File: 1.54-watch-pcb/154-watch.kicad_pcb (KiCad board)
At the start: 4 copper layers, 49.5 x 33 mm, 58 parts, among them J1 AFC24-S24FIC-00, J2 Conn_01x06_Female, J3 USB_C_Programming, J4 Jack-DC, J5 Conn_01x02_Male, Q1 Si1308, Q2 BC817, Q3 BC817, Q4 Si2301CDS, SW1 RESET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

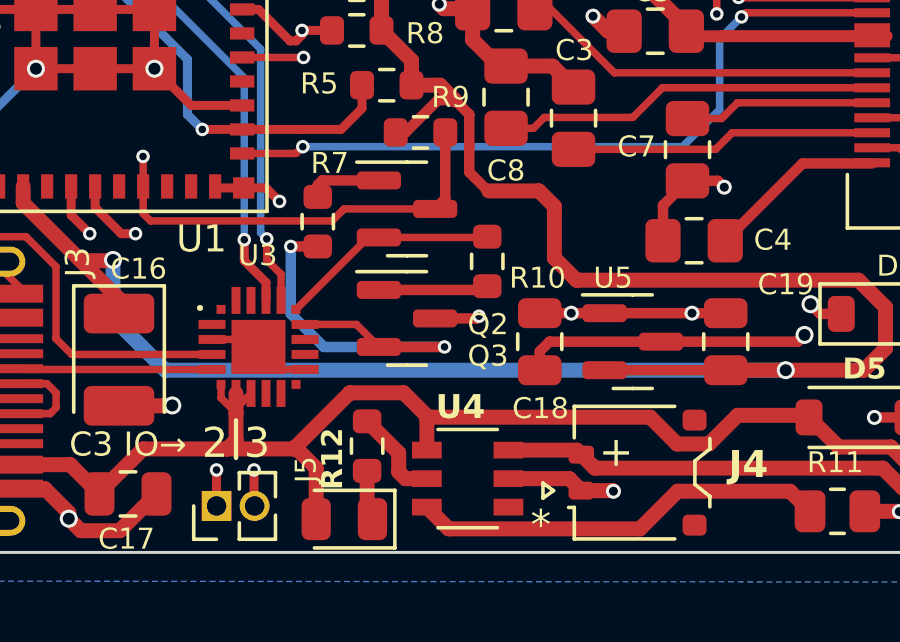
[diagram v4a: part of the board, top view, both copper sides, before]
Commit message: #6 Add a pull-down to power switch Q4
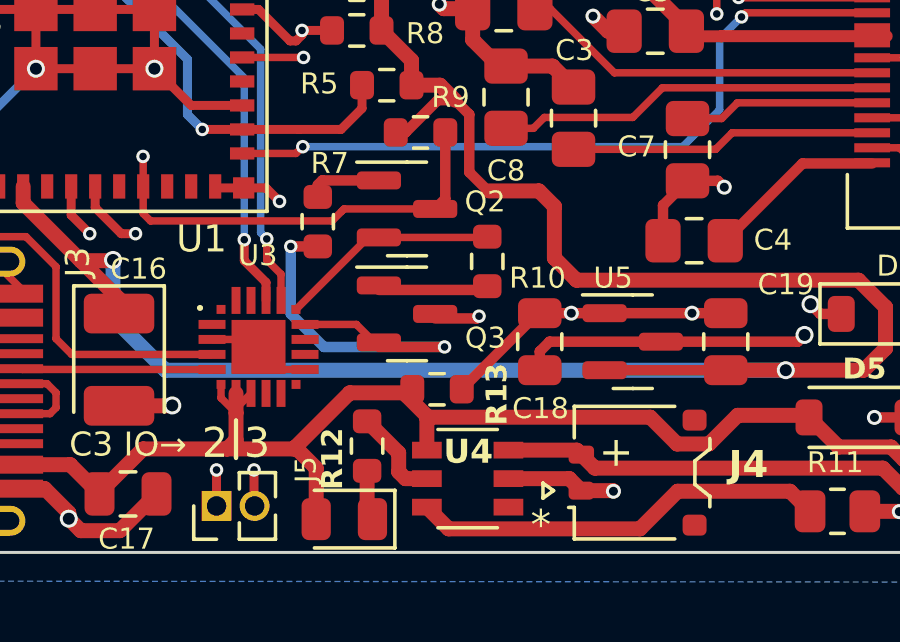
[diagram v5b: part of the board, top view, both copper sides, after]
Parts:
- added R13: 10K, Resistor_SMD:R_0603_1608Metric, F.Cu at (94.7, 57.1)
- moved Q3 0.15 mm to (93.7, 54.5)
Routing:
- net GND: track 101.2 -> 104.9 mm
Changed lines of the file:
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@@
     )
     (pad_to_mask_clearance 0)
-    (grid_origin 111.4 43.762)
     (pcbplotparams
       (layerselection 0x00010fc_ffffffff)
@@
   )
   (footprint "Package_TO_SOT_SMD:SOT-23" (layer "F.Cu")
-    (at 93.7 54.7)
+    (at 93.7 54.55)
     (descr "SOT, 3 Pin (https://www.jedec.org/system/files/docs/to-236h.pdf variant AB), generated with kicad-footprint-generator ipc_gullwing_generator.py")
     (tags "SOT TO_SOT_SMD")
@@
     (property "ki_keywords" "NPN Transistor")
     (attr smd)
-    (fp_text reference "Q3" (at 2.7 1.25) (layer "F.SilkS")
+    (fp_text reference "Q3" (at 2.61 0.8) (layer "F.SilkS")
         (effects (font (size 0.7 0.7) (thickness 0.13)))
     )
@@
     )
   )
+  (footprint "Resistor_SMD:R_0603_1608Metric" (layer "F.Cu")
+    (at 94.7 57.06 180)
+    (descr "Resistor SMD 0603 (1608 Metric), square (rectangular) end terminal, IPC_7351 nominal, (Body size source: IPC-SM-782 page 72, https://www.pcb-3d.com/wordpress/wp-content/uploads/ipc-sm-782a_amendment_1_and_2.pdf), generated with kicad-footprint-generator")
+    (tags "resistor")
+    (property "LCSC" "C25804")
+    (property "Sheetfile" "154-watch.kicad_sch")
+    (property "Sheetname" "")
+    (property "ki_description" "Resistor, small symbol")
+    (property "ki_keywords" "R resistor")
+    (attr smd)
+    (fp_text reference "R13" (at -1.99 -0.17 90) (layer "F.SilkS")
+        (effects (font (size 0.7 0.7) (thickness 0.13) bold))
+    )
+    (fp_text value "10K" (at 0 1.43) (layer "F.Fab")
+        (effects (font (size 1 1) (thickness 0.15)))
+    )
+    (fp_text user "${REFERENCE}" (at 0 0) (layer "F.Fab")
+        (effects (font (size 0.4 0.4) (thickness 0.06)))
+    )
+    (fp_line (start -0.237258 -0.5225) (end 0.237258 -0.5225)
+      (stroke (width 0.12) (type solid)) (layer "F.SilkS"))
+    (fp_line (start -0.237258 0.5225) (end 0.237258 0.5225)
+      (stroke (width 0.12) (type solid)) (layer "F.SilkS"))
+    (fp_line (start -1.48 -0.73) (end 1.48 -0.73)
+      (stroke (width 0.05) (type solid)) (layer "F.CrtYd"))
+    (fp_line (start -1.48 0.73) (end -1.48 -0.73)
+      (stroke (width 0.05) (type solid)) (layer "F.CrtYd"))
+    (fp_line (start 1.48 -0.73) (end 1.48 0.73)
+      (stroke (width 0.05) (type solid)) (layer "F.CrtYd"))
+    (fp_line (start 1.48 0.73) (end -1.48 0.73)
+      (stroke (width 0.05) (type solid)) (layer "F.CrtYd"))
+    (fp_line (start -0.8 -0.4125) (end 0.8 -0.4125)
+      (stroke (width 0.1) (type solid)) (layer "F.Fab"))
+    (fp_line (start -0.8 0.4125) (end -0.8 -0.4125)
+      (stroke (width 0.1) (type solid)) (layer "F.Fab"))
+    (fp_line (start 0.8 -0.4125) (end 0.8 0.4125)
+      (stroke (width 0.1) (type solid)) (layer "F.Fab"))
+    (fp_line (start 0.8 0.4125) (end -0.8 0.4125)
+      (stroke (width 0.1) (type solid)) (layer "F.Fab"))
+    (pad "1" smd roundrect (at -0.825 0 180) (size 0.8 0.95) (layers "F.Cu" "F.Paste" "F.Mask") (roundrect_rratio 0.25)
+      (net 2 "GND") (pintype "passive"))
+    (pad "2" smd roundrect (at 0.825 0 180) (size 0.8 0.95) (layers "F.Cu" "F.Paste" "F.Mask") (roundrect_rratio 0.25)
+      (net 3 "VBUS") (pintype "passive"))
+    (model "${KICAD6_3DMODEL_DIR}/Resistor_SMD.3dshapes/R_0603_1608Metric.wrl"
+      (offset (xyz 0 0 0))
+      (scale (xyz 1 1 1))
+      (rotate (xyz 0 0 0))
+    )
+  )
   (footprint "Capacitor_SMD:C_0805_2012Metric_Pad1.18x1.45mm_HandSolder" (layer "F.Cu")
     (at 97 47.325 -90)
@@
     (property "ki_keywords" "NPN Transistor")
     (attr smd)
-    (fp_text reference "Q2" (at 2.7 3.85) (layer "F.SilkS")
+    (fp_text reference "Q2" (at 2.6 -0.24) (layer "F.SilkS")
         (effects (font (size 0.7 0.7) (thickness 0.13)))
     )
@@
     (property "Sheetname" "")
     (attr smd)
-    (fp_text reference "U4" (at 0.24 2.39 180) (layer "F.SilkS")
+    (fp_text reference "U4" (at -0.0189 0.900001 180) (layer "F.SilkS")
         (effects (font (size 0.8 0.8) (thickness 0.14) bold))
     )
@@
   (segment (start 94.925 44.375) (end 94.775 44.225) (width 0.5) (layer "F.Cu") (net 2))
   (segment (start 80.845 53.875) (end 80.845 53.72) (width 0.25) (layer "F.Cu") (net 2))
+  (segment (start 98.06 54.525) (end 95.525 57.06) (width 0.35) (layer "F.Cu") (net 2))
   (segment (start 86.5 31.75) (end 86.75 32) (width 0.3) (layer "F.Cu") (net 2))
   (segment (start 89.55 38.45) (end 89.575 38.425) (width 0.35) (layer "F.Cu") (net 2))
@@
   (segment (start 80.845 53.72) (end 79.93 52.805) (width 0.25) (layer "F.Cu") (net 2))
   (segment (start 81.3301 42.425) (end 85.2801 42.425) (width 0.3) (layer "F.Cu") (net 2))
+  (segment (start 98.125 54.525) (end 98.06 54.525) (width 0.35) (layer "F.Cu") (net 2))
   (segment (start 80.2 36.45) (end 81.525 36.45) (width 0.25) (layer "F.Cu") (net 2))
   (segment (start 82.825 61.775) (end 82.425 61.375) (width 0.5) (layer "F.Cu") (net 2))

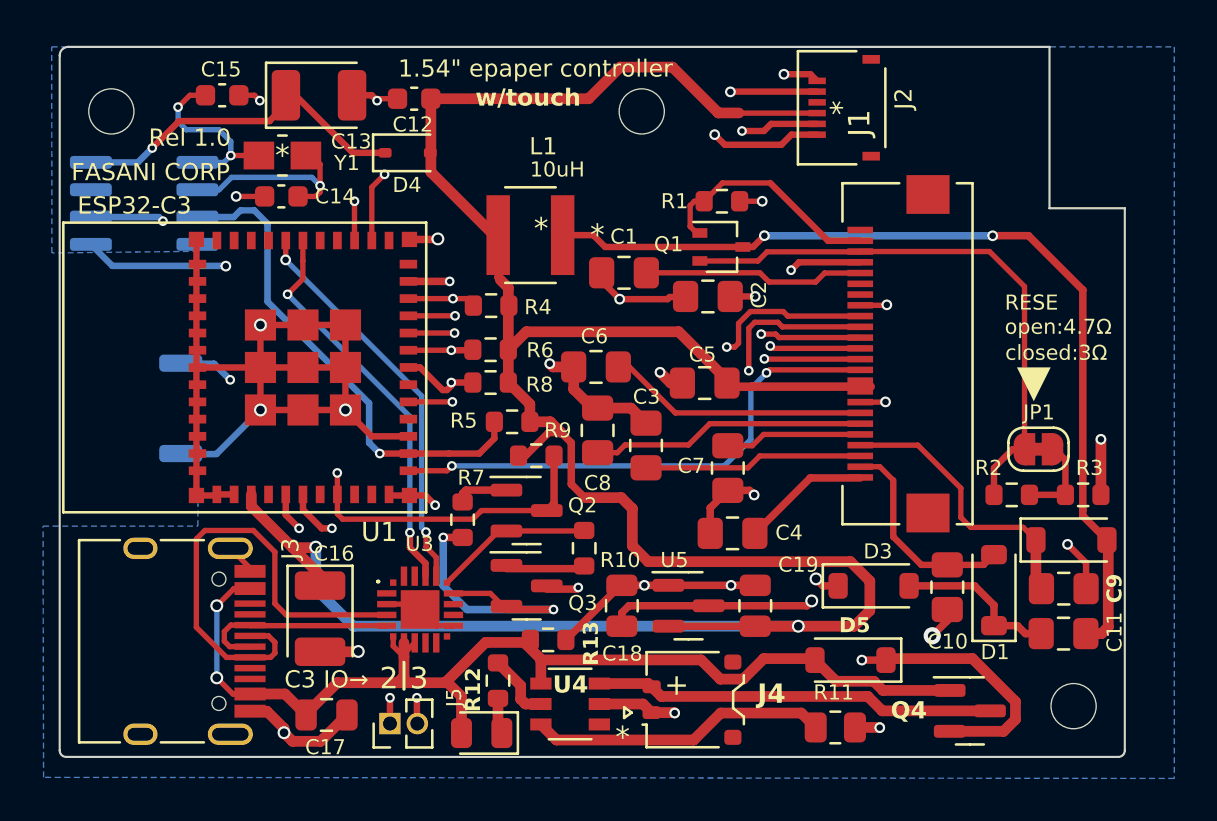
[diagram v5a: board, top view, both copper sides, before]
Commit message: Fix DRC 1.54 DRC
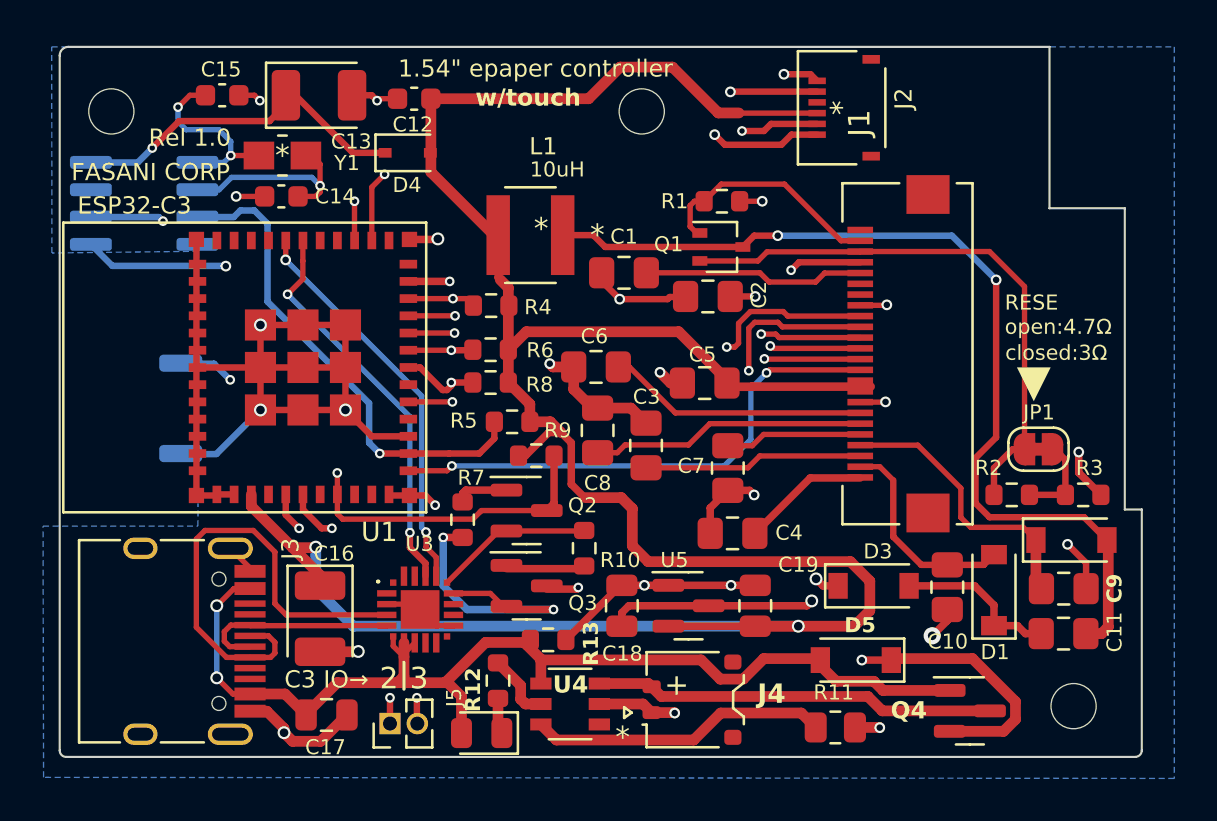
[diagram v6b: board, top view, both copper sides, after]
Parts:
- J1: value AFC24-S24FIC-00 -> CONN_AFC24-S24FIC-00_JUS
- U1: value ESP32-C3-MINI-1-N4 -> ESP32-C3-MINI
- U4: value TP4057-42-SOT26-R -> SOT-23-5_TPW
- moved D5 0.25 mm to (109.0, 58.0)
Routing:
- net Net-(D2-A): track 43.0 -> 44.3 mm
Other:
- board size 49.5 x 33 mm -> 50.3 x 33 mm

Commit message: 1.54 add QR code to this repo
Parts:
- moved SW1 3.58 mm to (76.1, 43.0), turned to 0 degrees
- moved H1 0.50 mm to (74.4, 32.0)
- moved H3 0.50 mm to (99.0, 32.0)
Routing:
- net GND: track 104.7 -> 100.2 mm
- net Net-(Q2-C): track 25.4 -> 29.5 mm
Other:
- board text added: "1"
- board text added: "200x200 PCF8563 RTC. I2C GPIOs: RTC_INT=2 | SDA=5 SCL=4 SPI GPIOs: MOSI=0 CLK=6 CS=19 RST=10 BUSY=7 DC=18"
- board text added: "24"
- board text added: "3 RST 4 VDD 5 SCL 6 SDA"
- board text added: "6"
- board text added: "TOUCH Pinup: 1 GND 2 INT"
- board text removed: "200x200 with optional touch panel PCF8563 RTC"
- board text removed: "3 RST 4 INT 5 SCL 6 SDA"
- board text removed: "TOUCH Pinup: 1 GND 2 VDD"
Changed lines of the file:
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@@
   )
   (footprint "MountingHole:MountingHole_2.1mm" (layer "F.Cu")
-    (at 74.4 32.5)
+    (at 74.4 32)
     (descr "Mounting Hole 2.1mm, no annular")
     (tags "mounting hole 2.1mm no annular")
@@
   )
   (footprint "MountingHole:MountingHole_2.1mm" (layer "F.Cu")
-    (at 99.05 32.5)
+    (at 99.05 32)
     (descr "Mounting Hole 2.1mm, no annular")
     (tags "mounting hole 2.1mm no annular")
@@
   )
   (footprint "footprint:Alps_SKRK" (layer "B.Cu")
-    (at 77.625 46.3 -90)
+    (at 76.13 43.05)
     (descr "http://www.alps.com/prod/info/E/HTML/Tact/SurfaceMount/SKRK/SKRKAHE020.html")
     (tags "SMD SMT button")
@@
     (property "ki_keywords" "switch normally-open pushbutton push-button")
     (attr smd)
-    (fp_text reference "SW1" (at 0 2.25 180) (layer "B.SilkS") hide
+    (fp_text reference "SW1" (at 0 2.25 90) (layer "B.SilkS") hide
         (effects (font (size 1 1) (thickness 0.15)) (justify mirror))
     )
-    (fp_text value "RESET" (at -0.075 2.75 90) (layer "B.Fab")
+    (fp_text value "RESET" (at -0.075 2.75) (layer "B.Fab")
         (effects (font (size 1 1) (thickness 0.15)) (justify mirror))
     )
-    (fp_text user "${REFERENCE}" (at 0 0 90) (layer "B.Fab")
+    (fp_text user "${REFERENCE}" (at 0 0) (layer "B.Fab")
         (effects (font (size 1 1) (thickness 0.15)) (justify mirror))
     )
@@
     (fp_circle (center 0 0) (end 1 0)
       (stroke (width 0.1) (type solid)) (fill none) (layer "B.Fab"))
-    (pad "1" smd roundrect (at -2.1 0 270) (size 0.8 2) (layers "B.Cu" "B.Paste" "B.Mask") (roundrect_rratio 0.25)
+    (pad "1" smd roundrect (at -2.1 0) (size 0.8 2) (layers "B.Cu" "B.Paste" "B.Mask") (roundrect_rratio 0.25)
       (net 45 "Net-(Q2-C)") (pinfunction "1") (pintype "passive"))
-    (pad "2" smd roundrect (at 2.1 0 270) (size 0.8 2) (layers "B.Cu" "B.Paste" "B.Mask") (roundrect_rratio 0.25)
+    (pad "2" smd roundrect (at 2.1 0) (size 0.8 2) (layers "B.Cu" "B.Paste" "B.Mask") (roundrect_rratio 0.25)
       (net 2 "GND") (pinfunction "2") (pintype "passive"))
     (model "${KIPRJMOD}/parts/3d/Button_SKRKAH.step"
@@
     (effects (font (size 0.8 0.8) (thickness 0.13)) (justify mirror))
   )
-  (gr_text "RST→" (at 83.15 46.35) (layer "B.SilkS")
+  (gr_text "RST→" (at 82.81 43.04) (layer "B.SilkS")
     (effects (font (size 0.8 0.8) (thickness 0.13)) (justify mirror))
   )
-  (gr_text "200x200\nwith optional touch panel\nPCF8563 RTC" (at 104.57 36.57) (layer "B.SilkS")
+  (gr_text "200x200\n\nPCF8563 RTC. I2C GPIOs:\nRTC_INT=2 | SDA=5 SCL=4\n\n\n\nSPI GPIOs:\nMOSI=0 CLK=6 CS=19\nRST=10 BUSY=7 DC=18" (at 109.86 39.16) (layer "B.SilkS")
     (effects (font (size 1 1) (thickness 0.15)) (justify left mirror))
   )
-  (gr_text "TOUCH Pinup: 1 GND 2 VDD" (at 104.59 40.21) (layer "B.SilkS")
+  (gr_text "TOUCH Pinup: 1 GND 2 INT" (at 109.98 51.26) (layer "B.SilkS")
     (effects (font (size 0.8 0.8) (thickness 0.13)) (justify left mirror))
   )
-  (gr_text "GOOD DISPLAY GDEY0154D67" (at 99.08 30.49) (layer "B.SilkS")
+  (gr_text "GOOD DISPLAY GDEY0154D67" (at 98.86869 30.49) (layer "B.SilkS")
     (effects (font (size 1 1) (thickness 0.15)) (justify mirror))
   )
-  (gr_text "3 RST 4 INT  5 SCL 6 SDA" (at 91.66 41.79) (layer "B.SilkS")
+  (gr_text "3 RST 4 VDD  5 SCL 6 SDA" (at 97.03 52.83) (layer "B.SilkS")
     (effects (font (size 0.8 0.8) (thickness 0.13)) (justify mirror))
   )
+  (gr_text "6" (at 104.82 34.27) (layer "F.SilkS")
+    (effects (font (size 0.8 0.8) (thickness 0.14) bold) (justify left bottom))
+  )
   (gr_text "▼" (at 116.48 45.9) (layer "F.SilkS")
     (effects (font (size 1.5 1.5) (thickness 0.14)) (justify left bottom))
@@
     (effects (font (size 0.7 0.7) (thickness 0.13)) (justify left))
   )
+  (gr_text "24" (at 106.45 38.48) (layer "F.SilkS")
+    (effects (font (size 0.8 0.8) (thickness 0.14) bold) (justify left bottom))
+  )
   (gr_text "C3 IO→" (at 84.4 58.9) (layer "F.SilkS")
     (effects (font (size 0.8 0.8) (thickness 0.13)))
   )
+  (gr_text "1" (at 104.82 31.17) (layer "F.SilkS")
+    (effects (font (size 0.8 0.8) (thickness 0.14) bold) (justify left bottom))
+  )
+  (gr_text "1" (at 107.211905 49.92) (layer "F.SilkS")
+    (effects (font (size 0.8 0.8) (thickness 0.14) bold) (justify left bottom))
+  )
   (gr_text "3" (at 88.7 58.85) (layer "F.SilkS")
     (effects (font (size 1 1) (thickness 0.15)))
@@
   (via (at 81.3301 42.425) (size 0.6) (drill 0.4) (layers "F.Cu" "B.Cu") (net 2))
   (via (at 89.45 50.8) (size 0.45) (drill 0.25) (layers "F.Cu" "B.Cu") (net 2))
-  (segment (start 79.2801 48.425) (end 81.3301 46.375) (width 0.3) (layer "B.Cu") (net 2))
-  (segment (start 79.2801 48.425) (end 77.65 48.425) (width 0.3) (layer "B.Cu") (net 2))
-  (segment (start 77.65 48.425) (end 77.625 48.4) (width 0.3) (layer "B.Cu") (net 2))
   (segment (start 101.8078 57.9922) (end 94.4022 57.9922) (width 0.5) (layer "F.Cu") (net 3))
   (segment (start 90.6725 59.6925) (end 90.6725 61.39) (width 0.5) (layer "F.Cu") (net 3))
@@
   (segment (start 79.3 55.475) (end 79.3 58.825) (width 0.25) (layer "B.Cu") (net 3))
   (segment (start 98.6125 50.9625) (end 98.6125 52.6875) (width 0.5) (layer "F.Cu") (net 4))
+  (segment (start 97.61 34.42) (end 97.66 34.42) (width 0.5) (layer "F.Cu") (net 4))
   (segment (start 96.425 50.45) (end 98.1 50.45) (width 0.5) (layer "F.Cu") (net 4))
   (segment (start 104.186137 45.296137) (end 103.183637 45.296137) (width 0.4) (layer "F.Cu") (net 4))
+  (segment (start 97.66 34.42) (end 95.15 31.91) (width 0.5) (layer "F.Cu") (net 4))
   (segment (start 100.2875 56.425) (end 104.325 56.425) (width 0.35) (layer "F.Cu") (net 4))
   (segment (start 92.85 40.7) (end 92.475 40.325) (width 0.5) (layer "F.Cu") (net 4))
@@
   (segment (start 103.0125 44.9825) (end 100.77 42.74) (width 0.5) (layer "F.Cu") (net 4))
   (segment (start 93.325 48.5) (end 93.65 48.5) (width 0.35) (layer "F.Cu") (net 4))
-  (segment (start 102.61 32.572) (end 103.57 32.572) (width 0.5) (layer "F.Cu") (net 4))
   (segment (start 103.578 32.58) (end 103.57 32.572) (width 0.25) (layer "F.Cu") (net 4))
+  (segment (start 89.25 31.91) (end 94.96 31.91) (width 0.5) (layer "F.Cu") (net 4))
   (segment (start 93.85 46.1) (end 93.85 46.925) (width 0.5) (layer "F.Cu") (net 4))
   (segment (start 109.65 55.7) (end 108.925 56.425) (width 0.5) (layer "F.Cu") (net 4))
@@
   (segment (start 80.9051 50.8551) (end 82.825 52.775) (width 0.5) (layer "F.Cu") (net 4))
   (segment (start 104.192274 45.29) (end 109.69 45.29) (width 0.4) (layer "F.Cu") (net 4))
+  (segment (start 97.66 34.42) (end 100.42 34.42) (width 0.5) (layer "F.Cu") (net 4))
   (segment (start 92.3778 40.2278) (end 92.475 40.325) (width 0.35) (layer "F.Cu") (net 4))
-  (segment (start 89.25 31.91) (end 96.58 31.91) (width 0.5) (layer "F.Cu") (net 4))
   (segment (start 84.1 54.05) (end 84.1 54.5375) (width 0.5) (layer "F.Cu") (net 4))
   (segment (start 92.3778 38.25) (end 92.3778 40.2278) (width 0.35) (layer "F.Cu") (net 4))
-  (segment (start 98.05 30.44) (end 100.478 30.44) (width 0.5) (layer "F.Cu") (net 4))
-  (segment (start 100.478 30.44) (end 102.61 32.572) (width 0.5) (layer "F.Cu") (net 4))
   (segment (start 108.925 56.425) (end 106.325 56.425) (width 0.5) (layer "F.Cu") (net 4))
   (segment (start 106.325 56.425) (end 104.325 56.425) (width 0.5) (layer "F.Cu") (net 4))
@@
   (segment (start 94.725 47.425) (end 95.3 47.425) (width 0.35) (layer "F.Cu") (net 4))
   (segment (start 82.825 52.775) (end 83.875 52.775) (width 0.5) (layer "F.Cu") (net 4))
+  (segment (start 95.15 31.91) (end 94.96 31.91) (width 0.5) (layer "F.Cu") (net 4))
   (segment (start 93.65 48.5) (end 94.725 47.425) (width 0.35) (layer "F.Cu") (net 4))
   (segment (start 92.85 45.1) (end 93.85 46.1) (width 0.5) (layer "F.Cu") (net 4))
+  (segment (start 102.268 32.572) (end 103.57 32.572) (width 0.5) (layer "F.Cu") (net 4))
   (segment (start 82.825 52.775) (end 84.1 54.05) (width 0.5) (layer "F.Cu") (net 4))
   (segment (start 83.875 52.775) (end 83.9 52.75) (width 0.5) (layer "F.Cu") (net 4))
   (segment (start 98.1 50.45) (end 98.6125 50.9625) (width 0.5) (layer "F.Cu") (net 4))
   (segment (start 92.85 45.1) (end 92.85 40.7) (width 0.5) (layer "F.Cu") (net 4))
-  (segment (start 96.58 31.91) (end 98.05 30.44) (width 0.5) (layer "F.Cu") (net 4))
+  (segment (start 100.42 34.42) (end 102.268 32.572) (width 0.5) (layer "F.Cu") (net 4))
   (segment (start 98.6125 52.6875) (end 99.35 53.425) (width 0.5) (layer "F.Cu") (net 4))
   (segment (start 93.85 46.925) (end 94.8 46.925) (width 0.5) (layer "F.Cu") (net 4))
@@
   (segment (start 82.975 44.975) (end 79.925 44.975) (width 0.25) (layer "In1.Cu") (net 45))
   (segment (start 84.9 46.9) (end 82.975 44.975) (width 0.25) (layer "In1.Cu") (net 45))
-  (segment (start 77.65 44.225) (end 77.625 44.2) (width 0.3) (layer "B.Cu") (net 45))
-  (segment (start 79.175 44.225) (end 77.65 44.225) (width 0.3) (layer "B.Cu") (net 45))
-  (segment (start 79.175 44.225) (end 79.925 44.975) (width 0.3) (layer "B.Cu") (net 45))
+  (segment (start 79.925 44.975) (end 75.955 44.975) (width 0.25) (layer "B.Cu") (net 45))
+  (segment (start 75.955 44.975) (end 74.03 43.05) (width 0.25) (layer "B.Cu") (net 45))
   (segment (start 96.25 53.75) (end 96.375 53.625) (width 0.35) (layer "F.Cu") (net 46))
   (segment (start 92.7625 53.75) (end 96.25 53.75) (width 0.35) (layer "F.Cu") (net 46))
